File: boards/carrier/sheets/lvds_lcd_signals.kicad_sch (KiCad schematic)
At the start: 6 parts, among them J5A FPC-05F-40PH20

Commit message: clean build: overlap=0 bounds=0 ERC=0 on all 27 sheets
Drives the carrier to a fully clean build — every sheet passes the
strict overlap/bounds validators AND KiCad ERC with 0 errors, nothing
hidden. Finishes the correctness + faithful-validators + placement
overhaul.

Geometry / placement (general algorithms, no per-block patches):

* _add_wire_with_bbox: partial-collinear-overlap clip. A new wire that
  partially overlaps an existing collinear wire (neither exact-dup nor
  subset) is clipped by interval-subtraction to its uncovered residual
  and meets the covering wire at a shared endpoint (validator-exempt,
  KiCad-merged). Removes the usb_pd doubled-trunk overlap; connectivity
  is preserved exactly.

* pick_dynamic_value_shift: generic fallback ladder. When a lib_id has
  no curated VALUE_SHIFT entry (connectors, power symbols, arbitrary
  ICs) the baseline is synthesised from the symbol's own library Value
  position (_library_value_shift), so the refinement can relocate ANY
  overlapping Value text. _refine_cluster_value_shifts now acts on every
  conflicting symbol except #PWR/#FLG (whose rail label is positional).
  Clears the jtag J2 part-name vs GND-symbol value overprint.

ERC errors 5 -> 0 (real electrical fixes, no rule suppression):

* PWR_FLAG Rule B (geometry-aware): the root index exposes no sheet
  pins, so hier-label nets are LOCAL per sub-sheet. Any DECLARED net
  carrying an IC power-INPUT pin (read from symbol pin TYPE), that is
  not a global power-symbol rail and has no local driver, now gets a
  local PWR_FLAG. Fixes power/usbc_otg +VIN (LDO/switch IN) and hdmi_rx
  VCCB (cable-side 5V sense). +3V3/+5V stay exempt (global, driven by a
  flag elsewhere).

* Decoupling-array eligibility is now per-part: a part whose from_pin
  has no NAMED net (e.g. the CP2102N reset pull-up onto bare ~{RST})
  stays clustered on its pin instead of being arrayed with an
  unlabelable terminal. Fixes uart_bridge R102 dangling pin.

* Connector cluster/array d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
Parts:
- removed R103: 100R, Resistor_SMD:R_0402_1005Metric, symbol Device:R
- removed R104: 100k, Resistor_SMD:R_0402_1005Metric, symbol Device:R
- R102: value 100R -> 100k
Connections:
- net LVDS_CLK- is gone; now on net GND: R102.1
- net ZYNQ_LCD_BL_EN: now also J5A.26 (BL_EN), R102.2
- net ZYNQ_LCD_EDID_SCL: now also J5A.5 (EDID_SCL), R101.2
- net ZYNQ_LCD_EDID_SDA: now also J5A.4 (EDID_SDA), R100.2
- net ZYNQ_LCD_LVDS_CLK_P: now also J5A.8 (LVDS_CLK+)
- net ZYNQ_LCD_LVDS_DA0_P: now also J5A.11 (LVDS_DATA0+)

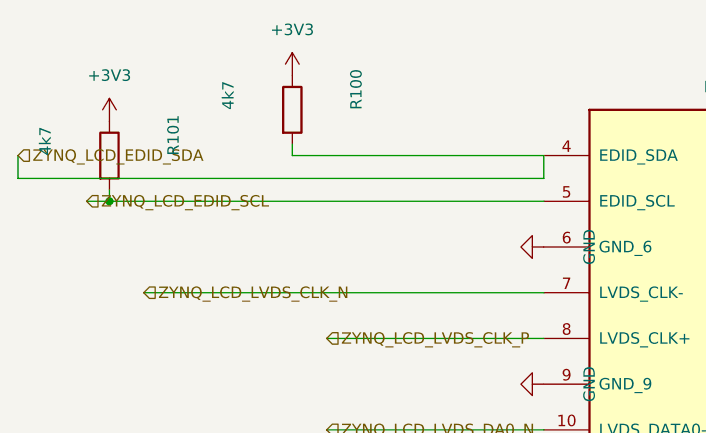
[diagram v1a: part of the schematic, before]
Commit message: Phase 1: render-truthful feedback loop (renderer + clearance validator + survey/reconcile)
The validator reported "clean" while sheets rendered crowded, and nothing
rendered the pages automatically — so each prior fix silently regressed
another sheet. This builds the measurement loop the rebuild needs.

- core/render/: kicad-cli→PDF→PNG renderer (raster.py) with exact mm→px
  transform; finding overlay (overlay.py); reconcile harness (reconcile.py);
  `python -m zynq_eda.core.render` CLI. pymupdf/pillow added as `render` extra.
- validate/overlap.py: enforce the 2mm VISUAL_CLEARANCE_MM breathing room
  (crowding) on visible-primitive pairs, not just true intersection. The
  validator only got stricter — no rule weakened. Wire-pair clearance is
  deferred to the routing rebuild (needs the net-attachment model).
  ValidationResult now carries bbox_a/bbox_b for the overlay. Dead code removed.
- layout/text_obstacles.py: single fail-loud source of truth for a symbol's
  text bboxes. plan.py no longer silently drops them on exception, and now
  includes reference_shift (matching the validator) — fixing a real divergence.
- pipeline.py/cli.py: --survey emits+validates all 27 sheets without halting,
  writes survey_report.md (measurement mode; gating build unchanged).
- tests: PageRaster transform + clearance gate/end-to-end.

Survey reveals 440 crowding findings across 27 sheets vs 3 with the old
intersection-only validator — the true state Phases 2-5 will drive to zero.
229 existing + 8 new unit tests pass.

Co-Authored-By: Claude Opus 4.8 <noreply@anthropic.com>
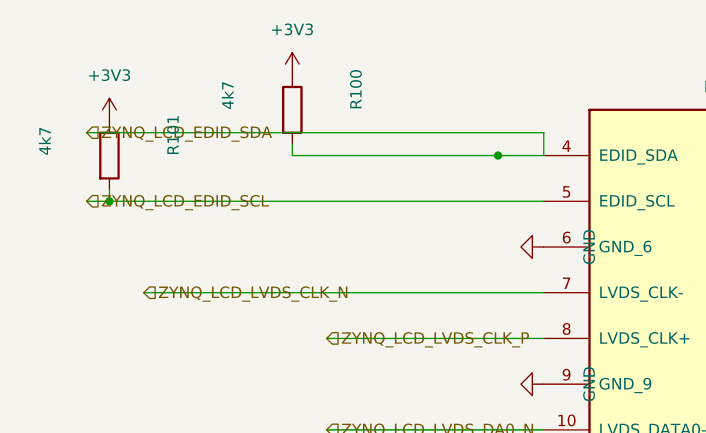
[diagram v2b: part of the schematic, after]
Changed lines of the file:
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@@
 		(instances
 			(project "LVDS LCD bank A (data + clock + backlight ctrl)"
-				(path "/b8bdd27e-b6ba-491d-97d0-44ded330f8d8"
+				(path "/67167e79-64fd-4c1d-8e7e-9e158308cc16"
 					(reference "J5A")
 					(unit 1)
@@
 		(instances
 			(project "LVDS LCD bank A (data + clock + backlight ctrl)"
-				(path "/b8bdd27e-b6ba-491d-97d0-44ded330f8d8"
+				(path "/67167e79-64fd-4c1d-8e7e-9e158308cc16"
 					(reference "#PWR200")
 					(unit 1)
@@
 		(instances
 			(project "LVDS LCD bank A (data + clock + backlight ctrl)"
-				(path "/b8bdd27e-b6ba-491d-97d0-44ded330f8d8"
+				(path "/67167e79-64fd-4c1d-8e7e-9e158308cc16"
 					(reference "#PWR201")
 					(unit 1)
@@
 		(instances
 			(project "LVDS LCD bank A (data + clock + backlight ctrl)"
-				(path "/b8bdd27e-b6ba-491d-97d0-44ded330f8d8"
+				(path "/67167e79-64fd-4c1d-8e7e-9e158308cc16"
 					(reference "#PWR202")
 					(unit 1)
@@
 		(instances
 			(project "LVDS LCD bank A (data + clock + backlight ctrl)"
-				(path "/b8bdd27e-b6ba-491d-97d0-44ded330f8d8"
+				(path "/67167e79-64fd-4c1d-8e7e-9e158308cc16"
 					(reference "#PWR203")
 					(unit 1)
@@
 		(instances
 			(project "LVDS LCD bank A (data + clock + backlight ctrl)"
-				(path "/b8bdd27e-b6ba-491d-97d0-44ded330f8d8"
+				(path "/67167e79-64fd-4c1d-8e7e-9e158308cc16"
 					(reference "#PWR204")
 					(unit 1)
@@
 		(instances
 			(project "LVDS LCD bank A (data + clock + backlight ctrl)"
-				(path "/b8bdd27e-b6ba-491d-97d0-44ded330f8d8"
+				(path "/67167e79-64fd-4c1d-8e7e-9e158308cc16"
 					(reference "#PWR205")
 					(unit 1)
@@
 		(instances
 			(project "LVDS LCD bank A (data + clock + backlight ctrl)"
-				(path "/b8bdd27e-b6ba-491d-97d0-44ded330f8d8"
+				(path "/67167e79-64fd-4c1d-8e7e-9e158308cc16"
 					(reference "#PWR206")
 					(unit 1)
@@
 		(instances
 			(project "LVDS LCD bank A (data + clock + backlight ctrl)"
-				(path "/b8bdd27e-b6ba-491d-97d0-44ded330f8d8"
+				(path "/67167e79-64fd-4c1d-8e7e-9e158308cc16"
 					(reference "R100")
 					(unit 1)
@@
 		(instances
 			(project "LVDS LCD bank A (data + clock + backlight ctrl)"
-				(path "/b8bdd27e-b6ba-491d-97d0-44ded330f8d8"
+				(path "/67167e79-64fd-4c1d-8e7e-9e158308cc16"
 					(reference "#PWR300")
 					(unit 1)
@@
 		(instances
 			(project "LVDS LCD bank A (data + clock + backlight ctrl)"
-				(path "/b8bdd27e-b6ba-491d-97d0-44ded330f8d8"
+				(path "/67167e79-64fd-4c1d-8e7e-9e158308cc16"
 					(reference "R101")
 					(unit 1)
@@
 		(instances
 			(project "LVDS LCD bank A (data + clock + backlight ctrl)"
-				(path "/b8bdd27e-b6ba-491d-97d0-44ded330f8d8"
+				(path "/67167e79-64fd-4c1d-8e7e-9e158308cc16"
 					(reference "#PWR301")
 					(unit 1)
@@
 		(instances
 			(project "LVDS LCD bank A (data + clock + backlight ctrl)"
-				(path "/b8bdd27e-b6ba-491d-97d0-44ded330f8d8"
+				(path "/67167e79-64fd-4c1d-8e7e-9e158308cc16"
 					(reference "R102")
 					(unit 1)
@@
 		(instances
 			(project "LVDS LCD bank A (data + clock + backlight ctrl)"
-				(path "/b8bdd27e-b6ba-491d-97d0-44ded330f8d8"
+				(path "/67167e79-64fd-4c1d-8e7e-9e158308cc16"
 					(reference "#PWR302")
 					(unit 1)
@@
 	(wire
 		(pts
-			(xy 374.65 95.25) (xy 374.65 97.79)
-		)
-		(stroke
-			(width 0)
-			(type default)
-		)
-	)
-	(wire
-		(pts
-			(xy 374.65 97.79) (xy 316.23 97.79)
-		)
-		(stroke
-			(width 0)
-			(type default)
-		)
-	)
-	(wire
-		(pts
-			(xy 316.23 97.79) (xy 316.23 95.25)
+			(xy 374.65 95.25) (xy 374.65 92.71)
+		)
+		(stroke
+			(width 0)
+			(type default)
+		)
+	)
+	(wire
+		(pts
+			(xy 374.65 92.71) (xy 323.85 92.71)
 		)
 		(stroke
@@
 			(type default)
 		)
+	)
+	(junction
+		(at 369.57 95.25)
+		(diameter 0)
+		(color 0 0 0 0)
 	)
 	(junction
@@
 	(hierarchical_label "ZYNQ_LCD_EDID_SDA"
 		(shape input)
-		(at 316.23 95.25 180)
-		(effects
-			(font
+		(at 323.85 92.71 180)
+		(effects
+			(font

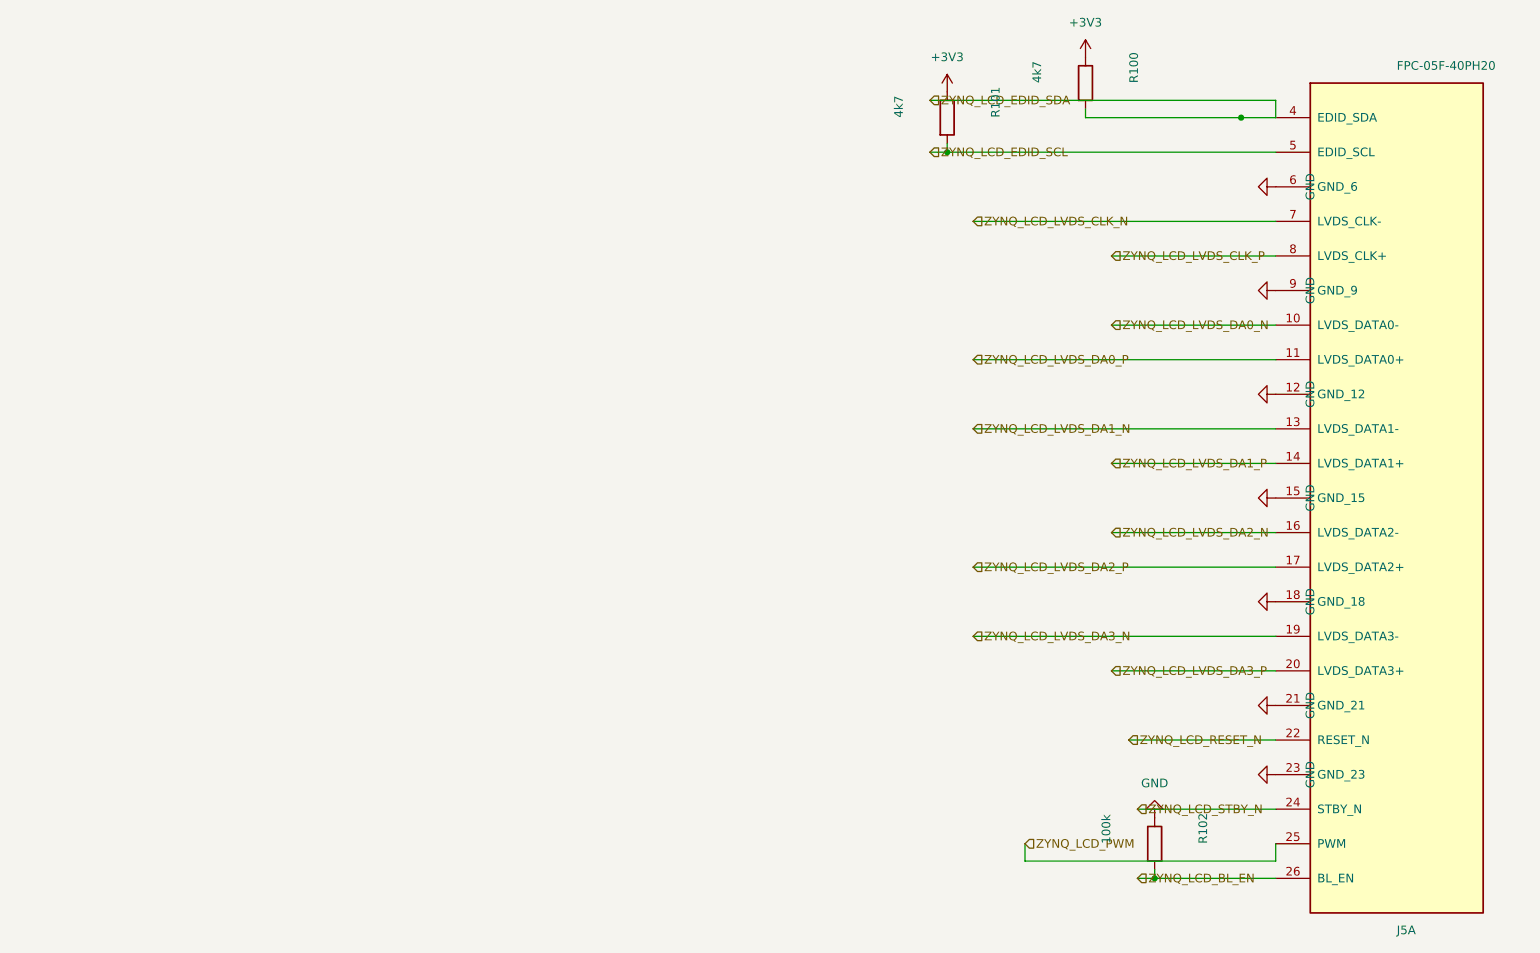
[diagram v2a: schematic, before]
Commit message: Regenerate carrier (overlap=0 all 27, ERC 134->22) + STAGE_E_STATUS UPDATE 4
Co-Authored-By: Claude Opus 4.8 <noreply@anthropic.com>
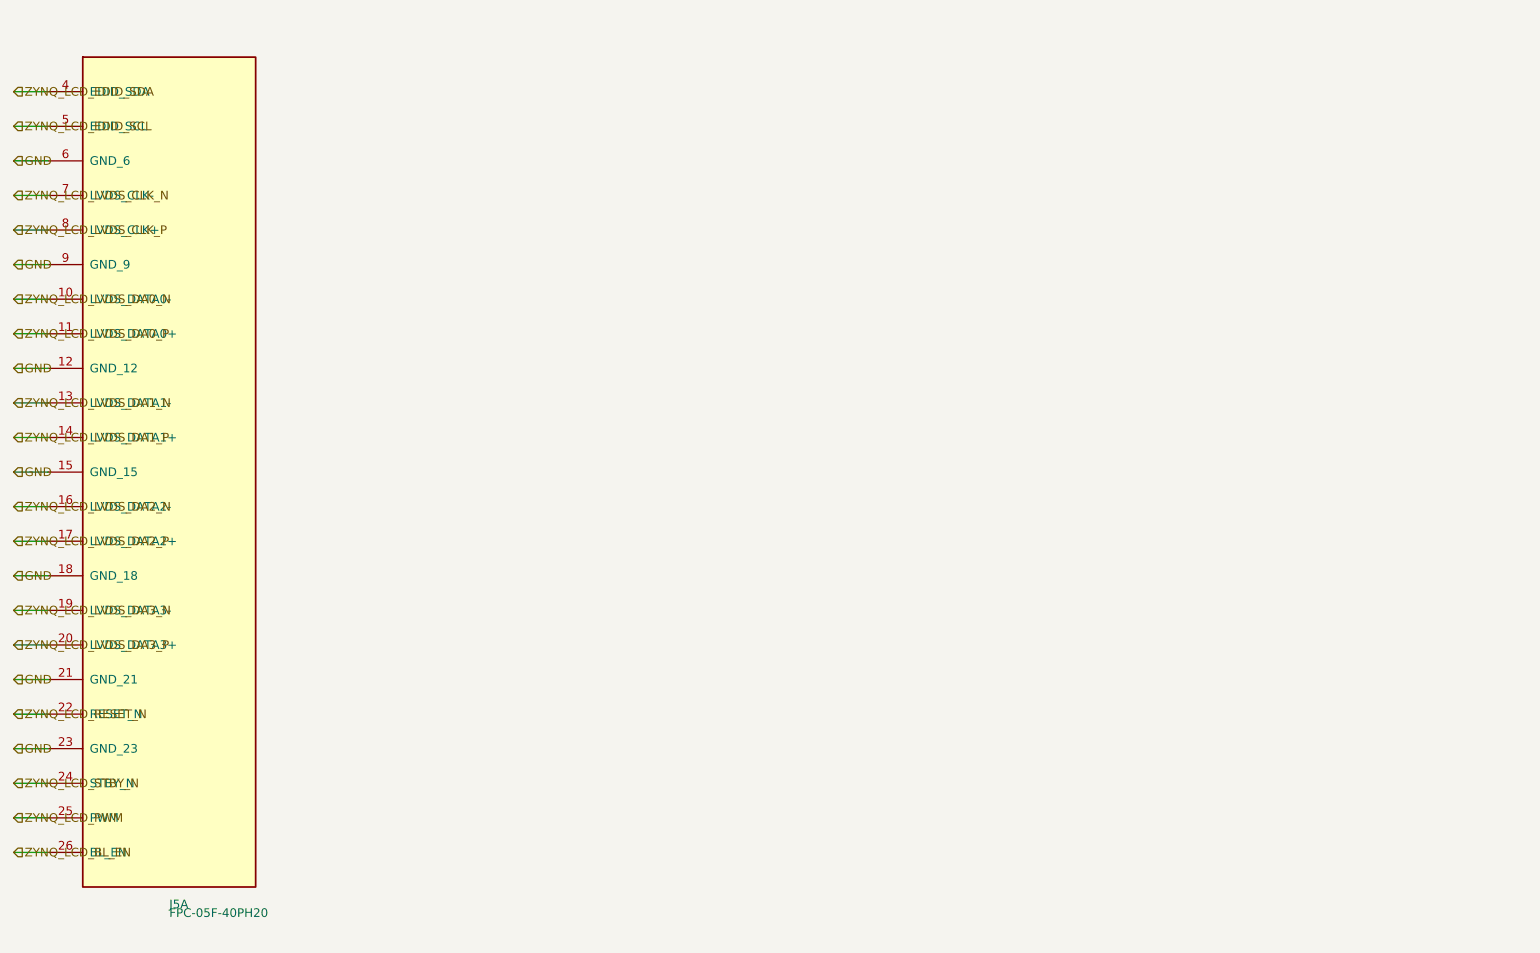
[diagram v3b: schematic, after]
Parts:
- removed R100, R101: 4k7, Resistor_SMD:R_0402_1005Metric, symbol Device:R
- removed R102: 100k, Resistor_SMD:R_0402_1005Metric, symbol Device:R
- J5A: LCSC C2856812 -> (none)
